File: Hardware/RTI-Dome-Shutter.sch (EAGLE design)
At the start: 42 parts, among them IC1 24AA128ST, IC5 74LVC245, IC6 74ABT245, J1 POWERPOLE_POWER45A

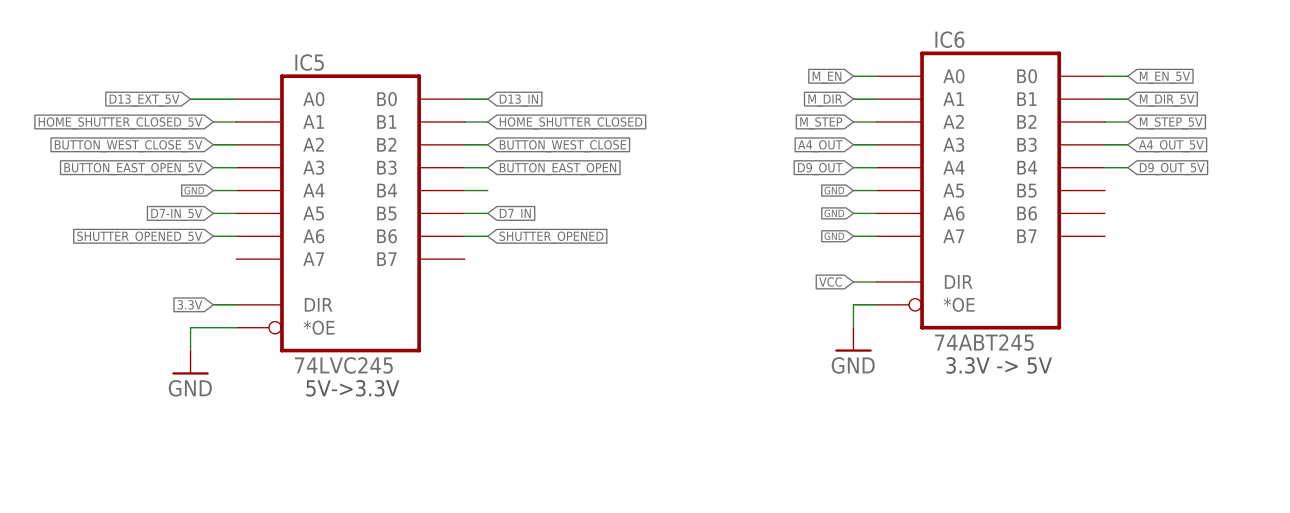
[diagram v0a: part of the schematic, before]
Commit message: Fix some board issue on the shutter
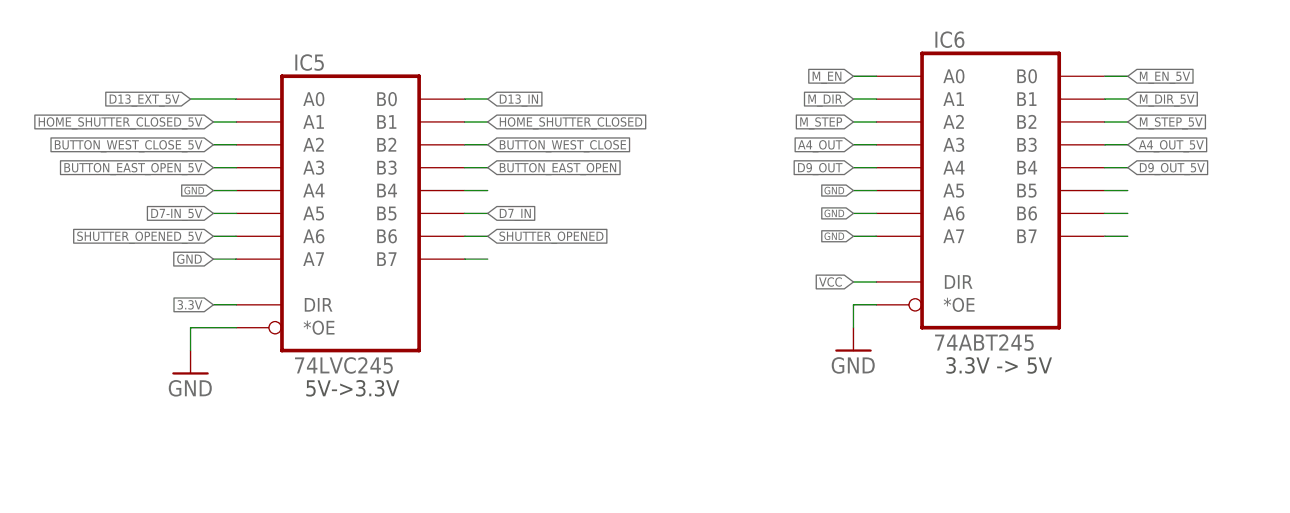
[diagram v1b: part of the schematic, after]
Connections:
- new net N$1: IC5G$1.B7
- new net N$6: IC6G$1.B5
- new net N$7: IC6G$1.B6
- new net N$8: IC6G$1.B7
- net GND: now also IC5G$1.A7
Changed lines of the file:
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@@
 <pinref part="GND11" gate="1" pin="GND"/>
+</segment>
+<segment>
+<pinref part="IC5" gate="G$1" pin="A7"/>
+<wire x1="116.84" y1="236.22" x2="119.38" y2="236.22" width="0.1524" layer="91"/>
+<label x="116.84" y="236.22" size="1.016" layer="95" rot="R180" xref="yes"/>
 </segment>
 </net>
@@
 </segment>
 </net>
+<net name="N$1" class="0">
+<segment>
+<pinref part="IC5" gate="G$1" pin="B7"/>
+<wire x1="147.32" y1="236.22" x2="144.78" y2="236.22" width="0.1524" layer="91"/>
+</segment>
+</net>
+<net name="N$6" class="0">
+<segment>
+<pinref part="IC6" gate="G$1" pin="B5"/>
+<wire x1="218.44" y1="243.84" x2="215.9" y2="243.84" width="0.1524" layer="91"/>
+</segment>
+</net>
+<net name="N$7" class="0">
+<segment>
+<pinref part="IC6" gate="G$1" pin="B6"/>
+<wire x1="218.44" y1="241.3" x2="215.9" y2="241.3" width="0.1524" layer="91"/>
+</segment>
+</net>
+<net name="N$8" class="0">
+<segment>
+<pinref part="IC6" gate="G$1" pin="B7"/>
+<wire x1="218.44" y1="238.76" x2="215.9" y2="238.76" width="0.1524" layer="91"/>
+</segment>
+</net>

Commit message: Re-did some of the core to receive data from network and wireless connection
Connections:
- net GND: now also R14.1
- net VCC: no longer R14.1
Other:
- moved on the sheet: R14
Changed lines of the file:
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@@
 <part name="GND11" library="supply1" deviceset="GND" device=""/>
 <part name="R11" library="rti" deviceset="R-EU" device="'0805'" value="100"/>
+<part name="GND13" library="supply1" deviceset="GND" device=""/>
 </parts>
 <sheets>
@@
 <instance part="P+4" gate="VCC" x="276.86" y="256.54"/>
 <instance part="R13" gate="G$1" x="312.42" y="241.3" rot="R90"/>
-<instance part="R14" gate="G$1" x="297.18" y="241.3" rot="R270"/>
+<instance part="R14" gate="G$1" x="292.1" y="175.26" rot="R270"/>
 <instance part="R15" gate="G$1" x="281.94" y="241.3" rot="R270"/>
 <instance part="R16" gate="G$1" x="289.56" y="241.3" rot="R270"/>
@@
 <instance part="GND11" gate="1" x="93.98" y="116.84"/>
 <instance part="R11" gate="G$1" x="83.82" y="132.08" rot="R180"/>
+<instance part="GND13" gate="1" x="279.4" y="175.26"/>
 </instances>
 <busses>
@@
 <label x="116.84" y="236.22" size="1.016" layer="95" rot="R180" xref="yes"/>
 </segment>
+<segment>
+<pinref part="R14" gate="G$1" pin="1"/>
+<wire x1="292.1" y1="180.34" x2="292.1" y2="185.42" width="0.1524" layer="91"/>
+<wire x1="292.1" y1="185.42" x2="279.4" y2="185.42" width="0.1524" layer="91"/>
+<wire x1="279.4" y1="185.42" x2="279.4" y2="177.8" width="0.1524" layer="91"/>
+<pinref part="GND13" gate="1" pin="GND"/>
+</segment>
 </net>
 <net name="+12V" class="1">
@@
 <net name="M_EN_5V" class="0">
 <segment>
-<label x="297.18" y="233.68" size="1.016" layer="95" rot="R270" xref="yes"/>
-<wire x1="297.18" y1="233.68" x2="297.18" y2="236.22" width="0.1524" layer="91"/>
+<label x="292.1" y="167.64" size="1.016" layer="95" rot="R270" xref="yes"/>
+<wire x1="292.1" y1="167.64" x2="292.1" y2="170.18" width="0.1524" layer="91"/>
 <pinref part="R14" gate="G$1" pin="2"/>
 </segment>
@@
 <wire x1="289.56" y1="246.38" x2="289.56" y2="248.92" width="0.1524" layer="91"/>
 <junction x="289.56" y="248.92"/>
-<pinref part="R14" gate="G$1" pin="1"/>
-<wire x1="297.18" y1="246.38" x2="297.18" y2="248.92" width="0.1524" layer="91"/>
-<junction x="297.18" y="248.92"/>
 <pinref part="R19" gate="G$1" pin="1"/>
 <wire x1="304.8" y1="246.38" x2="304.8" y2="248.92" width="0.1524" layer="91"/>

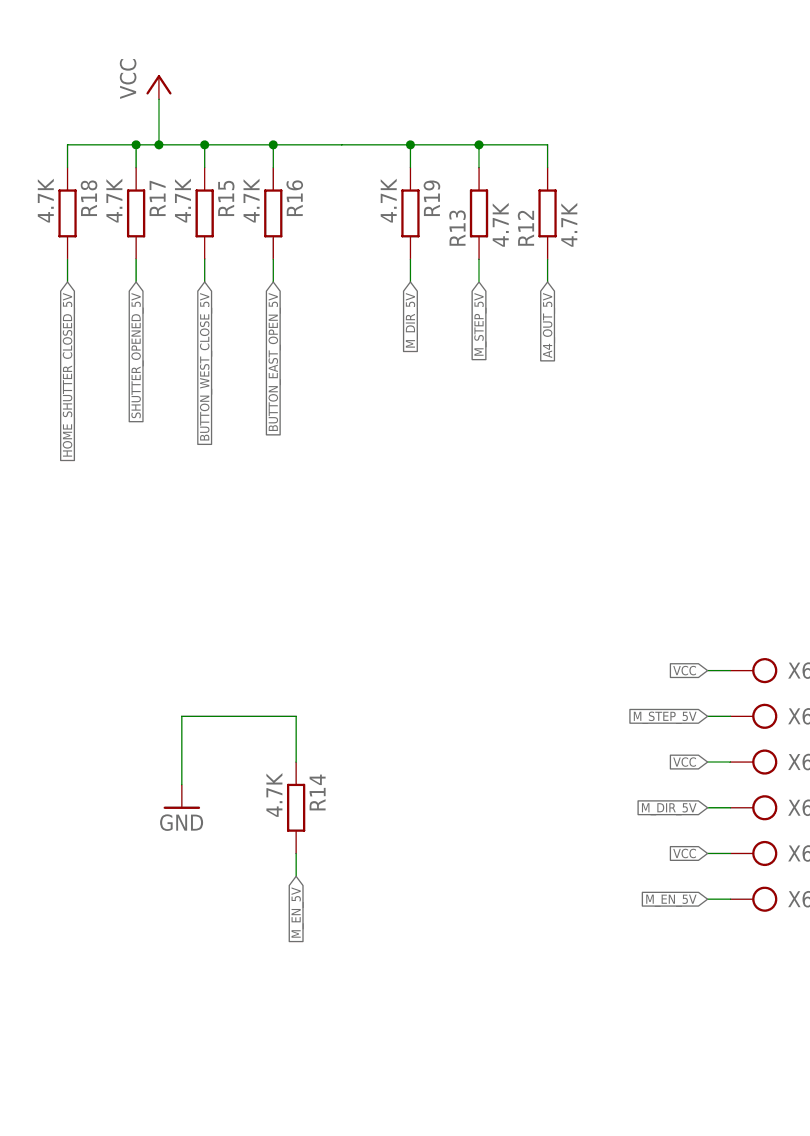
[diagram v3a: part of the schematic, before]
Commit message: Making some pull-up pull-down to get a better OFF state when the controller is not powered but the stepper driver is.
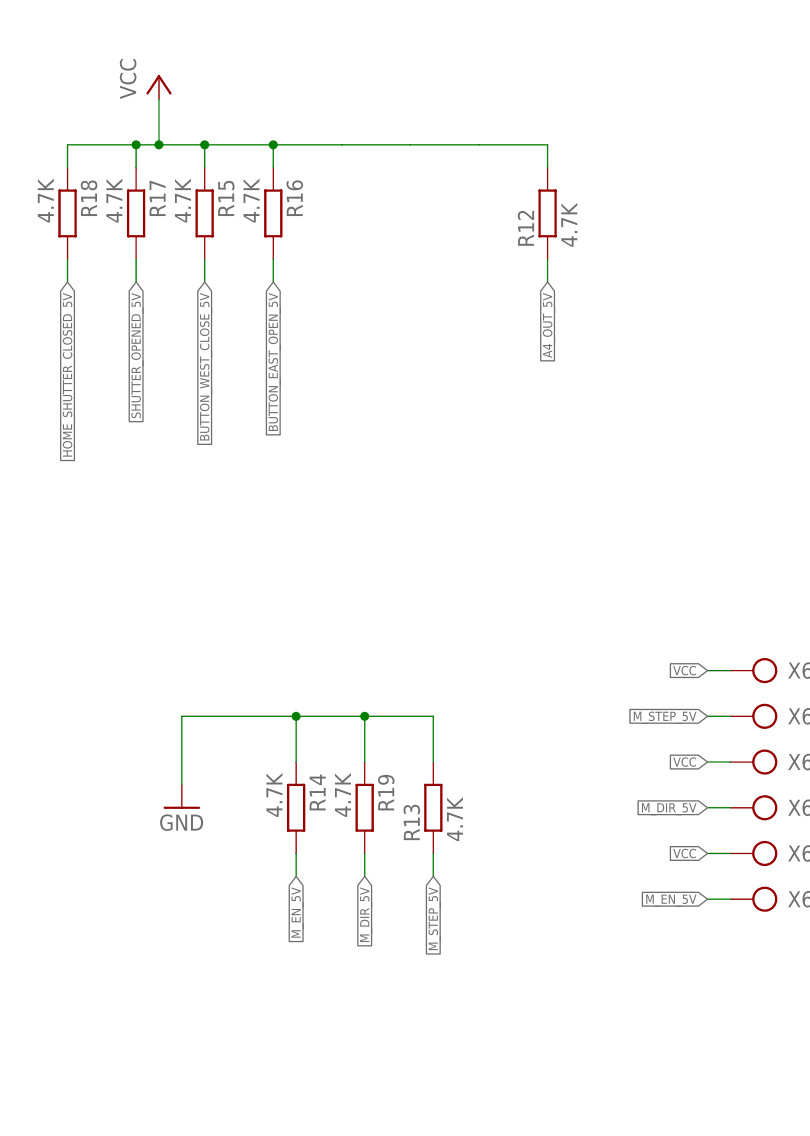
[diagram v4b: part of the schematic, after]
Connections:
- net GND: now also R13.2, R19.1
- net VCC: no longer R13.2, R19.1
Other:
- moved on the sheet: R13, R19
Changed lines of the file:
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@@
 <instance part="GND4" gate="1" x="368.3" y="45.72"/>
 <instance part="P+4" gate="VCC" x="276.86" y="256.54"/>
-<instance part="R13" gate="G$1" x="312.42" y="241.3" rot="R90"/>
+<instance part="R13" gate="G$1" x="307.34" y="175.26" rot="R90"/>
 <instance part="R14" gate="G$1" x="292.1" y="175.26" rot="R270"/>
 <instance part="R15" gate="G$1" x="281.94" y="241.3" rot="R270"/>
@@
 <instance part="R17" gate="G$1" x="274.32" y="241.3" rot="R270"/>
 <instance part="R18" gate="G$1" x="266.7" y="241.3" rot="R270"/>
-<instance part="R19" gate="G$1" x="304.8" y="241.3" rot="R270"/>
+<instance part="R19" gate="G$1" x="299.72" y="175.26" rot="R270"/>
 <instance part="R6" gate="G$1" x="7.62" y="195.58" rot="R90"/>
 <instance part="GND5" gate="1" x="7.62" y="182.88"/>
@@
 <wire x1="279.4" y1="185.42" x2="279.4" y2="177.8" width="0.1524" layer="91"/>
 <pinref part="GND13" gate="1" pin="GND"/>
+<pinref part="R13" gate="G$1" pin="2"/>
+<wire x1="292.1" y1="185.42" x2="299.72" y2="185.42" width="0.1524" layer="91"/>
+<wire x1="299.72" y1="185.42" x2="307.34" y2="185.42" width="0.1524" layer="91"/>
+<wire x1="307.34" y1="185.42" x2="307.34" y2="180.34" width="0.1524" layer="91"/>
+<junction x="292.1" y="185.42"/>
+<pinref part="R19" gate="G$1" pin="1"/>
+<wire x1="299.72" y1="185.42" x2="299.72" y2="180.34" width="0.1524" layer="91"/>
+<junction x="299.72" y="185.42"/>
 </segment>
 </net>
@@
 <net name="M_STEP_5V" class="0">
 <segment>
-<wire x1="312.42" y1="233.68" x2="312.42" y2="236.22" width="0.1524" layer="91"/>
-<label x="312.42" y="233.68" size="1.016" layer="95" rot="R270" xref="yes"/>
+<wire x1="307.34" y1="167.64" x2="307.34" y2="170.18" width="0.1524" layer="91"/>
+<label x="307.34" y="167.64" size="1.016" layer="95" rot="R270" xref="yes"/>
 <pinref part="R13" gate="G$1" pin="1"/>
 </segment>
@@
 <net name="M_DIR_5V" class="0">
 <segment>
-<label x="304.8" y="233.68" size="1.016" layer="95" rot="R270" xref="yes"/>
-<wire x1="304.8" y1="233.68" x2="304.8" y2="236.22" width="0.1524" layer="91"/>
+<label x="299.72" y="167.64" size="1.016" layer="95" rot="R270" xref="yes"/>
+<wire x1="299.72" y1="167.64" x2="299.72" y2="170.18" width="0.1524" layer="91"/>
 <pinref part="R19" gate="G$1" pin="2"/>
 </segment>
@@
 <wire x1="266.7" y1="246.38" x2="266.7" y2="248.92" width="0.1524" layer="91"/>
 <wire x1="266.7" y1="248.92" x2="274.32" y2="248.92" width="0.1524" layer="91"/>
-<pinref part="R13" gate="G$1" pin="2"/>
 <wire x1="274.32" y1="248.92" x2="276.86" y2="248.92" width="0.1524" layer="91"/>
 <wire x1="276.86" y1="248.92" x2="281.94" y2="248.92" width="0.1524" layer="91"/>
@@
 <wire x1="297.18" y1="248.92" x2="304.8" y2="248.92" width="0.1524" layer="91"/>
 <wire x1="304.8" y1="248.92" x2="312.42" y2="248.92" width="0.1524" layer="91"/>
-<wire x1="312.42" y1="248.92" x2="312.42" y2="246.38" width="0.1524" layer="91"/>
 <junction x="276.86" y="248.92"/>
 <pinref part="R17" gate="G$1" pin="1"/>
@@
 <wire x1="289.56" y1="246.38" x2="289.56" y2="248.92" width="0.1524" layer="91"/>
 <junction x="289.56" y="248.92"/>
-<pinref part="R19" gate="G$1" pin="1"/>
-<wire x1="304.8" y1="246.38" x2="304.8" y2="248.92" width="0.1524" layer="91"/>
-<junction x="304.8" y="248.92"/>
 <wire x1="312.42" y1="248.92" x2="320.04" y2="248.92" width="0.1524" layer="91"/>
-<junction x="312.42" y="248.92"/>
 <pinref part="R12" gate="G$1" pin="2"/>
 <wire x1="320.04" y1="248.92" x2="320.04" y2="246.38" width="0.1524" layer="91"/>

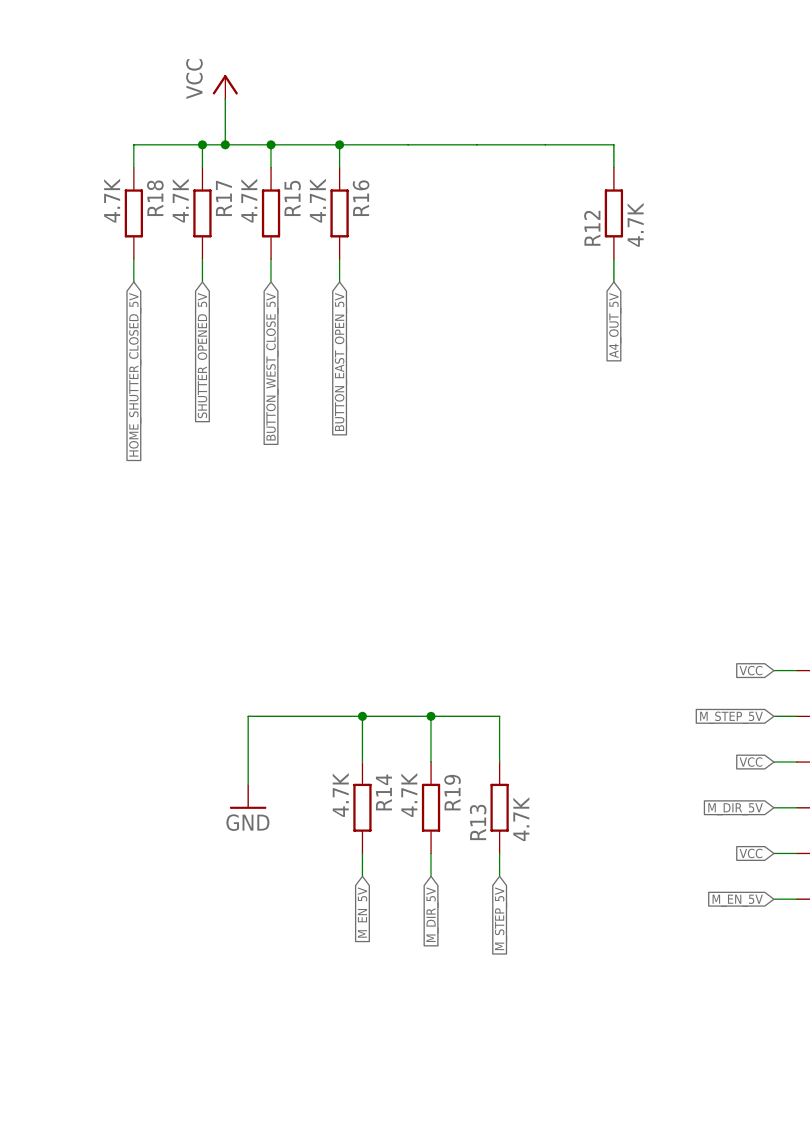
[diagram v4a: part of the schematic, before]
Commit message: Pull-down doesn't really help. Setting back to pull-up to make sure enable does enable :)
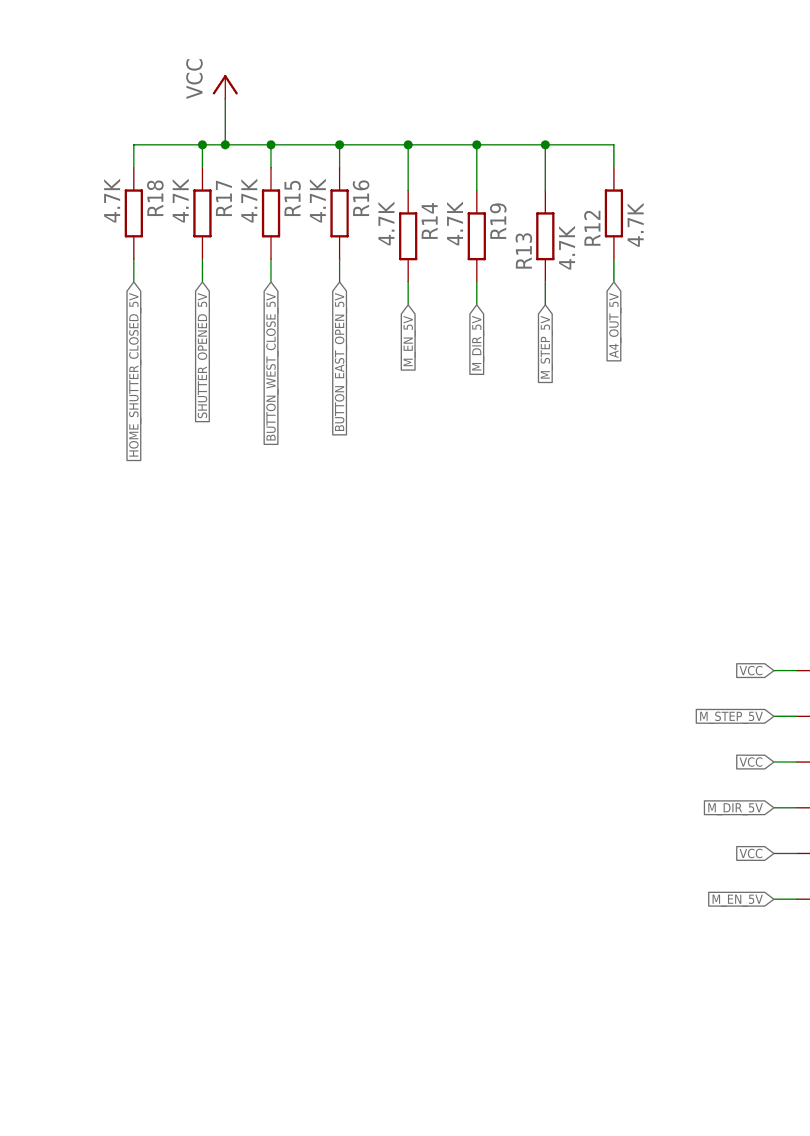
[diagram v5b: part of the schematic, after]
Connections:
- net GND: no longer R13.2, R14.1, R19.1
- net VCC: now also R13.2, R14.1, R19.1
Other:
- moved on the sheet: R13, R14, R19
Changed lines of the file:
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@@
 <part name="GND11" library="supply1" deviceset="GND" device=""/>
 <part name="R11" library="rti" deviceset="R-EU" device="'0805'" value="100"/>
-<part name="GND13" library="supply1" deviceset="GND" device=""/>
 </parts>
 <sheets>
@@
 <instance part="GND4" gate="1" x="368.3" y="45.72"/>
 <instance part="P+4" gate="VCC" x="276.86" y="256.54"/>
-<instance part="R13" gate="G$1" x="307.34" y="175.26" rot="R90"/>
-<instance part="R14" gate="G$1" x="292.1" y="175.26" rot="R270"/>
+<instance part="R13" gate="G$1" x="312.42" y="238.76" rot="R90"/>
+<instance part="R14" gate="G$1" x="297.18" y="238.76" rot="R270"/>
 <instance part="R15" gate="G$1" x="281.94" y="241.3" rot="R270"/>
 <instance part="R16" gate="G$1" x="289.56" y="241.3" rot="R270"/>
 <instance part="R17" gate="G$1" x="274.32" y="241.3" rot="R270"/>
 <instance part="R18" gate="G$1" x="266.7" y="241.3" rot="R270"/>
-<instance part="R19" gate="G$1" x="299.72" y="175.26" rot="R270"/>
+<instance part="R19" gate="G$1" x="304.8" y="238.76" rot="R270"/>
 <instance part="R6" gate="G$1" x="7.62" y="195.58" rot="R90"/>
 <instance part="GND5" gate="1" x="7.62" y="182.88"/>
@@
 <instance part="GND11" gate="1" x="93.98" y="116.84"/>
 <instance part="R11" gate="G$1" x="83.82" y="132.08" rot="R180"/>
-<instance part="GND13" gate="1" x="279.4" y="175.26"/>
 </instances>
 <busses>
@@
 <label x="116.84" y="236.22" size="1.016" layer="95" rot="R180" xref="yes"/>
 </segment>
-<segment>
-<pinref part="R14" gate="G$1" pin="1"/>
-<wire x1="292.1" y1="180.34" x2="292.1" y2="185.42" width="0.1524" layer="91"/>
-<wire x1="292.1" y1="185.42" x2="279.4" y2="185.42" width="0.1524" layer="91"/>
-<wire x1="279.4" y1="185.42" x2="279.4" y2="177.8" width="0.1524" layer="91"/>
-<pinref part="GND13" gate="1" pin="GND"/>
-<pinref part="R13" gate="G$1" pin="2"/>
-<wire x1="292.1" y1="185.42" x2="299.72" y2="185.42" width="0.1524" layer="91"/>
-<wire x1="299.72" y1="185.42" x2="307.34" y2="185.42" width="0.1524" layer="91"/>
-<wire x1="307.34" y1="185.42" x2="307.34" y2="180.34" width="0.1524" layer="91"/>
-<junction x="292.1" y="185.42"/>
-<pinref part="R19" gate="G$1" pin="1"/>
-<wire x1="299.72" y1="185.42" x2="299.72" y2="180.34" width="0.1524" layer="91"/>
-<junction x="299.72" y="185.42"/>
-</segment>
 </net>
 <net name="+12V" class="1">
@@
 <net name="M_STEP_5V" class="0">
 <segment>
-<wire x1="307.34" y1="167.64" x2="307.34" y2="170.18" width="0.1524" layer="91"/>
-<label x="307.34" y="167.64" size="1.016" layer="95" rot="R270" xref="yes"/>
+<wire x1="312.42" y1="231.14" x2="312.42" y2="233.68" width="0.1524" layer="91"/>
+<label x="312.42" y="231.14" size="1.016" layer="95" rot="R270" xref="yes"/>
 <pinref part="R13" gate="G$1" pin="1"/>
 </segment>
@@
 <net name="M_DIR_5V" class="0">
 <segment>
-<label x="299.72" y="167.64" size="1.016" layer="95" rot="R270" xref="yes"/>
-<wire x1="299.72" y1="167.64" x2="299.72" y2="170.18" width="0.1524" layer="91"/>
+<label x="304.8" y="231.14" size="1.016" layer="95" rot="R270" xref="yes"/>
+<wire x1="304.8" y1="231.14" x2="304.8" y2="233.68" width="0.1524" layer="91"/>
 <pinref part="R19" gate="G$1" pin="2"/>
 </segment>
@@
 <net name="M_EN_5V" class="0">
 <segment>
-<label x="292.1" y="167.64" size="1.016" layer="95" rot="R270" xref="yes"/>
-<wire x1="292.1" y1="167.64" x2="292.1" y2="170.18" width="0.1524" layer="91"/>
+<label x="297.18" y="231.14" size="1.016" layer="95" rot="R270" xref="yes"/>
+<wire x1="297.18" y1="231.14" x2="297.18" y2="233.68" width="0.1524" layer="91"/>
 <pinref part="R14" gate="G$1" pin="2"/>
 </segment>
@@
 <pinref part="R12" gate="G$1" pin="2"/>
 <wire x1="320.04" y1="248.92" x2="320.04" y2="246.38" width="0.1524" layer="91"/>
-</segment>
-<segment>
+<pinref part="R14" gate="G$1" pin="1"/>
+<wire x1="297.18" y1="243.84" x2="297.18" y2="248.92" width="0.1524" layer="91"/>
+<junction x="297.18" y="248.92"/>
+<pinref part="R19" gate="G$1" pin="1"/>
+<wire x1="304.8" y1="248.92" x2="304.8" y2="243.84" width="0.1524" layer="91"/>
+<junction x="304.8" y="248.92"/>
+<pinref part="R13" gate="G$1" pin="2"/>
+<wire x1="312.42" y1="248.92" x2="312.42" y2="243.84" width="0.1524" layer="91"/>
+<junction x="312.42" y="248.92"/>
+</segment>
+<segment>
